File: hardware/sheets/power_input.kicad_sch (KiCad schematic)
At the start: 16 parts, among them J1 PWR (SS1.5 3-way), Q1 SQJ415EP

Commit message: hw(sch): Task 7 schematic review - three defects found and fixed
Every spec requirement traced to a sheet and refdes, read back from the
exported netlist rather than the drawing. 29 of 31 rows PASS; two carried
forward. Full write-up in hardware/docs/schematic-review.md.

F1 - Q1 carried the superseded SQJ415EP. That part was replaced by the
SQJ461EP on 2026-09-13 precisely because it is a 40 V device and the
SMBJ24A clamps at 38.9 V - 2.8% margin on the one part that sees every
vehicle transient. The replacement reached part-selection.md and the spec
but never the schematic, so a BOM built from it would have ordered the
wrong FET. Also closes the open gate-drive question: D1/R1 put Vgs at
-11 to -12.6 V, so the 16 mOhm column applies and the 0.78 W figure stands.

F2 - R2 and R3, the 0R links that short both windings of the common-mode
choke L2, were not marked DNP. A BOM would have stuffed the choke AND the
links; the links win and L2 becomes decorative. The board would work
perfectly and filter nothing, with no ERC or DRC check saying a word.
Both are now DNP, and gen_power_input.py learned to emit (dnp yes).

F3 - the 24 V feedback divider (115k/4.99k = 120k) conducts in deep sleep:
with the boost disabled, +24V still sits at ~12.35 V through L3 and D4, so
the divider drew 103 uA - larger than every other sleep contributor
combined, and absent from the spec 8.2 budget. Raised to 576k/24.9k, same
ratio, 20.5 uA. Revised budget ~94 uA typ / ~111 uA max against the 200 uA
target. C61 (10 pF, DNP) fitted as a Cff stuff option for the higher FB
impedance.

Carried forward: F4 (L1/L2 carry the full 7.0 A and have no thermal budget
- a 22 mOhm total DCR ceiling is now specified) and F5 (the spec's second
feed DNP footprints do not exist; needs a decision before Task 8 commits
to an outline).

Verification: ERC --severity-all --exit-code-violations exit=0, 0 errors,
0 warnings. 166 nets, unchanged by the fixes. DNP set read back from the
sheets: 31 parts. All six genera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
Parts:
- Q1: value SQJ415EP -> SQJ461EP
- R2, R3: now not fitted
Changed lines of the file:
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@@
 		(on_board yes)
 		(in_pos_files yes)
-		(dnp no)
+		(dnp yes)
 		(property "Reference" "R3"
 			(at 92.71 92.71 90)
@@
 			)
 		)
-		(property "Value" "SQJ415EP"
+		(property "Value" "SQJ461EP"
 			(at 44.45 88.9 90)
 			(show_name no)
@@
 		(on_board yes)
 		(in_pos_files yes)
-		(dnp no)
+		(dnp yes)
 		(property "Reference" "R2"
 			(at 74.93 65.41 90)

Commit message: hw(sch): L2 = Wurth WE-CMBNC 7448031002, L1 = 1.5 uH - decision applied to the schematic
Owner's call: the Wurth over the two ferrite candidates. It is the only
AEC-Q200 Grade 1 part of the three and the only one that leaves the thermal
budget real margin - 18.40 mOhm against F4's 22 mOhm ceiling (16.4%) versus
21.80 mOhm (0.9%) for either ferrite, 0.90 W instead of 1.07 W, night total
~2.70 W against the plate's ~2.9 W.

Applied to the DESIGN, not just the prose: layout_power_input.py now sets
L2 = 7448031002 and L1 = 1.5uH, replacing the "CM choke" and "10uH"
placeholders. This is exactly what finding F1 caught going wrong the other
way - the SQJ461EP was chosen on 2026-09-13, recorded in three documents, and
never reached the generator, so a BOM built from the schematic would have
ordered a 40 V part.

The coupling between L1 and L2 is now written into the generator as a comment,
because it is not visible from either value alone: F4 caps L1 plus BOTH L2
windings at 22 mOhm, and with either ferrite alternative a 2.2 uH L1 breaks
the ceiling. Nobody should change one without re-checking the other.

Verification: ERC --severity-all --exit-code-violations exit=0, 0 violations.
166 nets, unchanged - these are Value fields, not connectivity. L1 and L2 read
back from the netlist as 1.5uH and 7448031002.

Still carried, both flagged rather than assumed: whether the Wurth's 6.3 mOhm
is per winding (assumed - conservative) or total, and the derating curve at
the 65 C internal ambient since the 10 A is specified at 20 C.

Co-Authored-By: Claude Opus 5 <noreply@anthropic.com>
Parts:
- L1: value 10uH -> 1.5uH
- L2: value CM choke -> 7448031002
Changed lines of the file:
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@@
 			)
 		)
-		(property "Value" "10uH"
+		(property "Value" "1.5uH"
 			(at 107.95 82.55 90)
 			(show_name no)
@@
 			)
 		)
-		(property "Value" "CM choke"
+		(property "Value" "7448031002"
 			(at 88.9 69.85 0)
 			(show_name no)

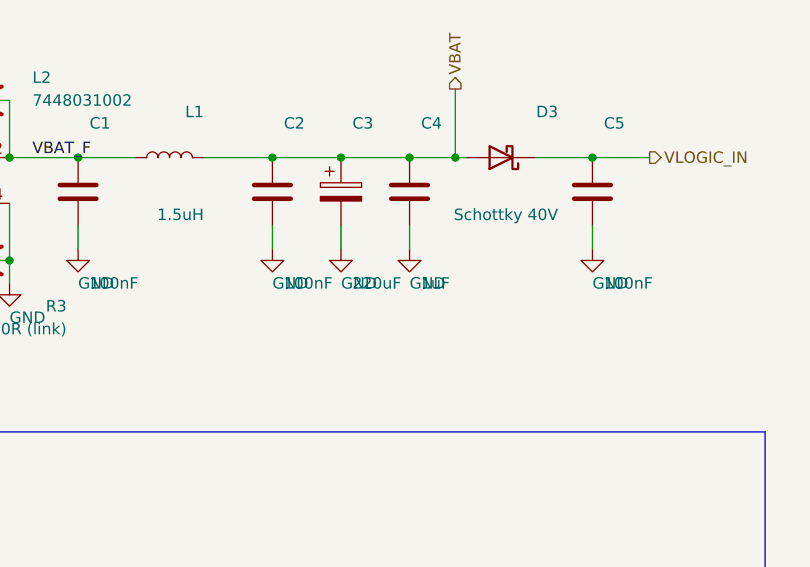
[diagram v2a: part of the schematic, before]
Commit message: hw(sch): sweep every selected part into the schematic; D6+D7 become one PESD2CANFD24U-T
Closes the gap the Task 7 review's finding F1 was about: parts chosen in
prose had not reached the generators, which is exactly how the superseded
SQJ415EP survived five days in the schematic.

STRUCTURAL - the CAN ESD pair is now one part. D6 and D7 were two placeholder
"24V bidir" discretes; the Nexperia PESD2CANFD24U-T is a single SOT23 holding
both bidirectional elements (K1/K2/CC). New verified symbol in symlib.py built
from Table 2 of the datasheet, added to gen_mcu_can's lib_symbols, and
Device:D_TVS dropped from that sheet since D6/D7 were its only users.

The two protected pins land exactly on the CANH and CANL runs, so each run is
drawn as TWO segments meeting AT the pin rather than one segment the pin
happens to touch. A pin sitting mid-wire does connect, but this project has
already produced one silent connectivity defect of that shape (labels
mid-wire, 14 instances), so the pin is made a wire endpoint and junctioned.
Verified from the netlist rather than from ERC: D6.1 -> /CANH, D6.2 -> /CANL,
D6.3 -> GND.

Consolidating freed D7, so the diode series was renumbered to stay gapless:
the ignition-divider BAT54 D8 -> D7, the twelve RGB sense clamps D9-D20 ->
D8-D19, and the PROFET sense clamp D21 -> D20. Every designator series is
gapless: C1-61, D1-20, F1-5, J1-8, L1-6, Q1-9, R1-99, SW1-2, U1-9.

VALUE SWEEP - L4/L5 "22uH" -> XAL7070-223ME, L6 "51uH CM choke" ->
ACT45B-510-2P-TL003, C3 "220uF" -> "220uF 63V" (the SMBJ24A's 8/20 us clamp is
50.6 V, so a 50 V part has no margin), U7 -> PCA9685PW/Q900, the only
AEC-Q100 variant in the ordering table. U7's lib_id stays Driver_LED:PCA9685PW
- that is the stock symbol's name, and the package is the same TSSOP28. D4 was
already SS5PH102.

FOOTPRINT - installed the vendor SamacSys footprint and STEP model for the
Wurth choke as footprints/mccan.pretty/Wurth_WE-CMBNC_7448031002.kicad_mod and
3dmodels/. Its pads verify against t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
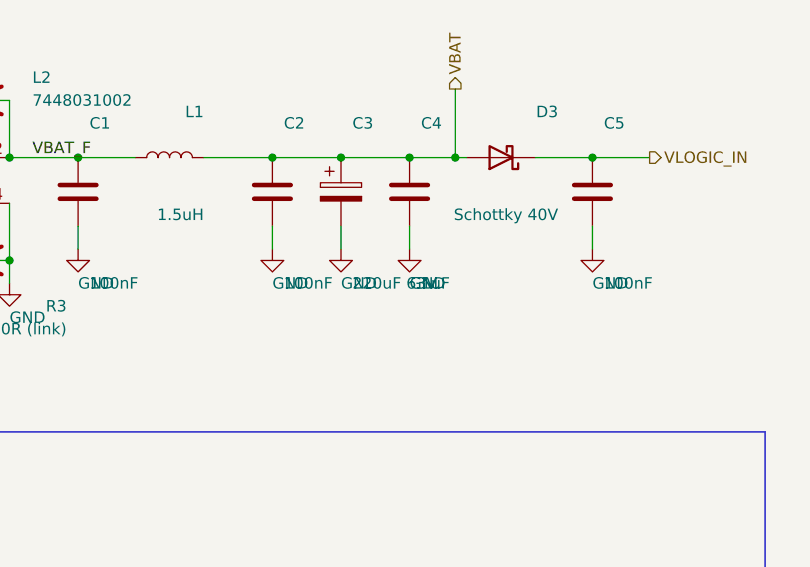
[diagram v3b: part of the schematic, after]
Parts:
- C3: value 220uF -> 220uF 63V
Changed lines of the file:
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@@
 			)
 		)
-		(property "Value" "220uF"
+		(property "Value" "220uF 63V"
 			(at 124.46 90.17 0)
 			(show_name no)

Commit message: hw(pcb): Task 8 step 0 - footprints assigned, 209 of 219 verified
Nothing in the project had a footprint except the PROFET's. Assignment now
lives in one auditable place, scripts/fpmap.py, which the four sheet
generators call when emitting each symbol's Footprint property. No generator
chooses a footprint of its own any more.

Three rules, and the reasoning is in the file rather than in a commit nobody
will read again: signal passives are 0603; a passive gets a bigger package
only for a stated reason; and nothing gets a footprint that has not been
checked to exist.

The reasons that drove a larger package:
- R2/R3, the 0R links bypassing the input choke windings, are 2512. They are
  DNP, but if anyone fits them for the tied-ground prototype they carry the
  entire 7.0 A night load, and a 0603 link is rated about 1 A.
- R52-R63, the RGB sense shunts, are 1206 for the FAULT case, not the normal
  7 mW. The package is sized on the understanding that firmware latches a
  shorted channel off; if that is ever dropped they must become 2512 1 W.
- The front-end ceramics are sized against the SMBJ24A's 8/20 us clamp of
  50.6 V, not the 38.9 V the distributor summaries quote. 100 nF fits 0805 at
  100 V; 1-2.2 uF at 63 V does not fit 0805; 10 uF at 63 V needs 1210.
- C20-C22 on +24 V are 1206 for DC-BIAS derating, a different reason - a 25 V
  X7R at 24 V keeps only 40-60% of nameplate.

Package identifications read from the datasheets rather than assumed:
NX5020UNBKS is SOT363/SC-88 (section 1), LM51571-Q1 RTE is WQFN-16 3x3 with a
1.66 mm exposed pad (so KiCad's EP1.675x1.675 is within tolerance), SS5PH102
is TO-277A, PESD2CANFD24U-T is SOT23.

FLAGGED, not silently accepted: the LM5164 DDA thermal pad is 3.4 x 2.8 mm on
the mechanical drawing and KiCad has no exact match. EP2.62x3.51 is the
closest by area (9.20 mm2 against 9.52) and is used for now, but that pad is
the part's heatsink on a thermally critical rail, so an exact DDA land pattern
should be drawn before fabr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
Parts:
- C1: footprint (none) -> Capacitor_SMD:C_0603_1608Metric
- C2, C5: footprint (none) -> Capacitor_SMD:C_0805_2012Metric
- C3: footprint (none) -> Capacitor_SMD:CP_Elec_10x10.5
- C4: footprint (none) -> Capacitor_SMD:C_1206_3216Metric
- D1: footprint (none) -> Diode_SMD:D_SOD-123
- D2: footprint (none) -> Diode_SMD:D_SMB
- D3: footprint (none) -> Diode_SMD:D_SMA
- L1: footprint (none) -> Inductor_SMD:L_Vishay_IHLP-4040
- L2: footprint (none) -> mccan:Wurth_WE-CMBNC_7448031002
- Q1: footprint (none) -> Package_SO:PowerPAK_SO-8L_Single
- R1: footprint (none) -> Resistor_SMD:R_0603_1608Metric
- R2, R3: footprint (none) -> Resistor_SMD:R_2512_6332Metric
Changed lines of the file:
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@@
 			)
 		)
-		(property "Footprint" ""
+		(property "Footprint" "Diode_SMD:D_SOD-123"
 			(at 62.23 85.09 0)
 			(hide yes)
@@
 			)
 		)
-		(property "Footprint" ""
+		(property "Footprint" "Capacitor_SMD:C_0603_1608Metric"
 			(at 93.98 80.01 0)
 			(hide yes)
@@
 			)
 		)
-		(property "Footprint" ""
+		(property "Footprint" "Diode_SMD:D_SMA"
 			(at 140.97 76.2 0)
 			(hide yes)
@@
 			)
 		)
-		(property "Footprint" ""
+		(property "Footprint" "Resistor_SMD:R_2512_6332Metric"
 			(at 81.28 87.63 0)
 			(hide yes)
@@
 			)
 		)
-		(property "Footprint" ""
+		(property "Footprint" "Capacitor_SMD:C_0805_2012Metric"
 			(at 151.13 80.01 0)
 			(hide yes)
@@
 			)
 		)
-		(property "Footprint" ""
+		(property "Footprint" "Resistor_SMD:R_0603_1608Metric"
 			(at 54.61 92.71 0)
 			(hide yes)
@@
 			)
 		)
-		(property "Footprint" ""
+		(property "Footprint" "Inductor_SMD:L_Vishay_IHLP-4040"
 			(at 104.14 76.2 0)
 			(hide yes)
@@
 			)
 		)
-		(property "Footprint" ""
+		(property "Footprint" "Capacitor_SMD:CP_Elec_10x10.5"
 			(at 123.19 80.01 0)
 			(hide yes)
@@
 			)
 		)
-		(property "Footprint" ""
+		(property "Footprint" "Capacitor_SMD:C_0805_2012Metric"
 			(at 115.57 80.01 0)
 			(hide yes)
@@
 			)
 		)
-		(property "Footprint" ""
+		(property "Footprint" "Package_SO:PowerPAK_SO-8L_Single"
 			(at 54.61 78.74 0)
 			(hide yes)
@@
 			)
 		)
-		(property "Footprint" ""
+		(property "Footprint" "Diode_SMD:D_SMB"
 			(at 66.04 80.01 0)
 			(hide yes)
@@
 			)
 		)
-		(property "Footprint" ""
+		(property "Footprint" "Resistor_SMD:R_2512_6332Metric"
 			(at 81.28 69.85 0)
 			(hide yes)
@@
 			)
 		)
-		(property "Footprint" ""
+		(property "Footprint" "Capacitor_SMD:C_1206_3216Metric"
 			(at 130.81 80.01 0)
 			(hide yes)
@@
 			)
 		)
-		(property "Footprint" ""
+		(property "Footprint" "mccan:Wurth_WE-CMBNC_7448031002"
 			(at 81.28 78.74 0)
 			(hide yes)

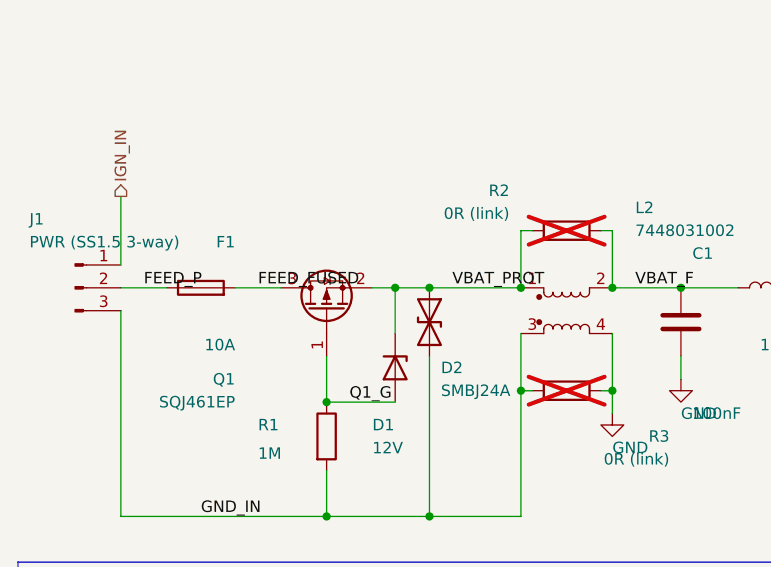
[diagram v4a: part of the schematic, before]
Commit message: hw(sch): CM chokes were wired to KiCad's pin numbering, not the parts'
Both common-mode chokes used Device:L_Coupled, which numbers its pins
winding A = 1-2, winding B = 3-4.  Every real four-terminal CM choke numbers
them winding A = 1-4, winding B = 2-3.  Both parts in this design are real
ones, so both were wired across the wrong pairs.

L2 was the serious one.  As drawn, winding 1-4 tied VBAT_PROT to board GND
and winding 2-3 tied VBAT_F to GND_IN -- two dead shorts across the supply
through 6.3 mOhm windings.  First power-up would have cleared the 10 A fuse
with the P-FET and the choke carrying the fault.

L6 transposed CANH and CANL between the transceiver and the connector, so the
board would never have received a frame.  Being listen-only by default, the
symptom is "no traffic" -- which spec 8.3 already names as the top risk and
the thing most likely to be misdiagnosed as a firmware fault.

ERC passes either way.  DRC passes either way.  The footprint pad count
matches either way.  Nothing automated catches this.

Verified from the VECTOR GEOMETRY of both datasheets, not a text dump -- a
flat extraction gives four bare numerals with no axis:
  Wurth WE-CMBNC 7448031002 "Schematic": upper coil's leads sit under labels
    1 (x=347.0) and 4 (x=488.6); lower coil's under 2 and 3 at the same x.
  TDK ACT45B "CIRCUIT DIAGRAM": identical, 1/4 upper, 2/3 lower.

Fix is a mccan_parts:CM_CHOKE_4T symbol drawn with L_Coupled's own graphics
but numbered to match the parts.  Not one wire moves -- which is also why the
drawing never looked wrong.  Netlist now reads:
  L2.1->4  VBAT_PROT -> VBAT_F      L2.2->3  GND_IN -> GND
  L6.1->4  U6 CANH   -> CANH        L6.2->3  U6 CANL -> CANL

Also in this commit, from the two datasheets supplied today:

- Superseal is a WIRE-TO-WIRE series with no panel-mount board-side housing,
  so the seven "panel connectors" could never have been built, and that is
  why all seven sat in fpmap.BLOCKED through Task 8 step 0.  J1 and J3-J8
  b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
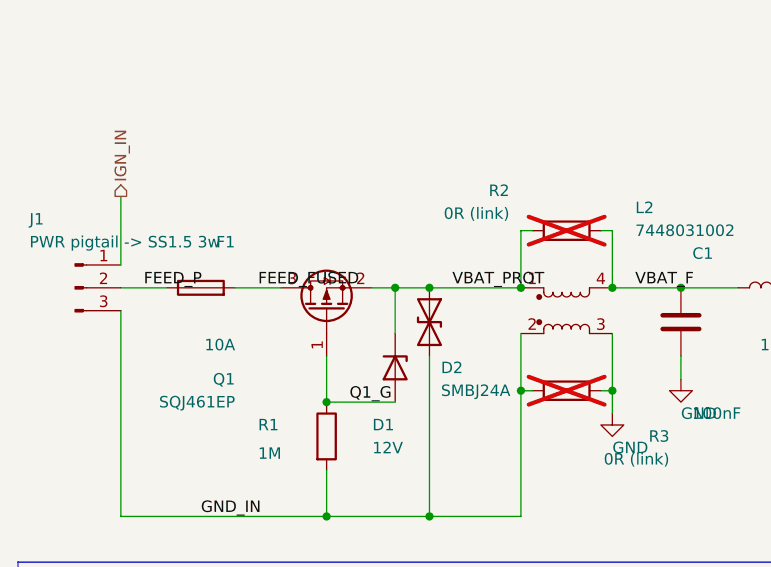
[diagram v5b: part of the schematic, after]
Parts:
- J1: value PWR (SS1.5 3-way) -> PWR pigtail -> SS1.5 3w; footprint (none) -> Connector_Wire:SolderWire-1.5sqmm_1x03_P6mm_D1.7mm_OD3mm_Relief
- L2: symbol Device:L_Coupled -> mccan_parts:CM_CHOKE_4T
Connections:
- net GND: now also L2.3; no longer L2.4
- net GND_IN: now also L2.2; no longer L2.3
- net VBAT_F: now also L2.4; no longer L2.2
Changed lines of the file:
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@@
 			)
 		)
-		(property "Value" "PWR (SS1.5 3-way)"
+		(property "Value" "PWR pigtail -> SS1.5 3w"
 			(at 21.59 71.12 0)
 			(show_name no)
@@
 			)
 		)
-		(property "Footprint" ""
+		(property "Footprint" "Connector_Wire:SolderWire-1.5sqmm_1x03_P6mm_D1.7mm_OD3mm_Relief"
 			(at 26.67 76.2 0)
 			(hide yes)
@@
 	)
 	(symbol
-		(lib_id "Device:L_Coupled")
+		(lib_id "mccan_parts:CM_CHOKE_4T")
 		(at 81.28 78.74 0)
 		(unit 1)

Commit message: hw(sch): spec 4.2 built - LTC4380 eFuse replaces F1/Q1/D1/R1
The input stage's fuse, P-FET, gate Zener and gate pull-down are gone. In
their place: U10 (LTC4380-2) driving a back-to-back pass pair Q10/Q11 across
R100, doing reverse polarity, current limit and overvoltage clamp in one
conduction path. Night falls 2.70 W -> 2.31 W.

Built from the datasheet's Figure 7, not Figure 5 - only R_SNS, R_DRN and
C_TMR are rescaled. Two deliberate departures, both noted on the sheet:
R103/C64 are the PIN FUNCTIONS minimum (33R/47nF) rather than Figure 7's
drawn 150R/0.1uF, because a larger C64 pushes the fault timeout past the SOA
curve that was checked; and ON/FLT are left open under no-connect flags.

THE PASS PAIR IS COMMON DRAIN. Verified by hand against the generated
netlist, which is what spec 4.2 makes the acceptance criterion:

  FEED_P     J1.2 Q10.2 Q12.2 R104.1 R105.1
  MID        Q10.3 Q11.3 R101.1
  SNS        Q11.2 R100.1 U10.4

Drains (pin 3) meet at MID, sources (pin 2) face outward. Wired common
source the board passes ERC, DRC and the pad count with no reverse-polarity
protection at all.

RENUMBERED. Spec 4.2 named its parts R88-R95, C49-C52 and D22-D24; every one
was taken - R88-R99 and C49-C61 are the RGB output snubbers. Built as
R100-R107, C62-C65 and D21-D23, and the spec now carries the mapping table.

C65 (22 uF at OUT) is new: PIN FUNCTIONS requires it and nothing else on the
sheet satisfied it. No orderable yet - flagged, along with Q12, D21-D23 and
the HSOF-8 variant for Q10/Q11.

Sheet moved to A3 and the input filter shifted 73.66 mm right to make room.
Note boxes now stack automatically in two columns rather than by hand.

ERC: 0 violations. Footprints: 233 verified, 0 failures, U4 still blocked.

Co-Authored-By: Claude Opus 5 <noreply@anthropic.com>
Claude-Session: https://claude.ai/code/session_01Bkq7QP4he4cdfxkUNzx7DL
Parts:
- removed D1: 12V, Diode_SMD:D_SOD-123, symbol Device:D_Zener
- removed F1: 10A, symbol Device:Fuse
- removed Q1: SQJ461EP, Package_SO:PowerPAK_SO-8L_Single, symbol Transistor_FET:Q_PMOS_GSD
- removed R1: 1M, Resistor_SMD:R_0603_1608Metric, symbol Device:R
- added C62: 680nF, Capacitor_SMD:C_0603_1608Metric, symbol Device:C
- added C63: 220nF, Capacitor_SMD:C_0603_1608Metric, symbol Device:C
- added C64: 47nF, Capacitor_SMD:C_0805_2012Metric, symbol Device:C
- added C65: 22uF 63V, Capacitor_SMD:CP_Elec_6.3x7.7, symbol Device:C_Polarized
- added D21: 22V, Diode_SMD:D_SOD-123, symbol Device:D_Zener
- added D22, D23: 1N4148, Diode_SMD:D_SOD-323, symbol Device:D
- added Q10, Q11: IPT008N06NM5LF, Package_TO_SOT_SMD:Infineon_PG-HSOF-8-1, symbol Transistor_FET:Q_NMOS_GSD
- added Q12: MMBT3904, Package_TO_SOT_SMD:SOT-23, symbol Transistor_BJT:Q_NPN_BEC
- added R100: 5m6 1% 1W, Resistor_SMD:R_2512_6332Metric, symbol Device:R
- added R101: 30k, Resistor_SMD:R_1206_3216Metric, symbol Device:R
- added R102: 10R, Resistor_SMD:R_0603_1608Metric, symbol Device:R
- added R103: 33R, Resistor_SMD:R_0603_1608Metric, symbol Device:R
- added R104, R106: 10k, Resistor_SMD:R_0603_1608Metric, symbol Device:R
- added R105, R107: 240k, Resistor_SMD:R_1206_3216Metric, symbol Device:R
- added U10: LTC4380HMS-2, Package_SO:MSOP-10_3x3mm_P0.5mm, symbol mccan_parts:LTC4380
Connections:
- net FEED_P: now also Q10.2 (S), Q12.2 (E), R104.1, R105.1
- net GND_IN: now also C62.2, C63.2, C64.2, C65.2, D21.2 (A), D23.2 (A), U10.6 (SEL), U10.8 (GND)
- net VBAT_PROT: now also C65.1, R100.2, U10.5 (OUT)
- new net: D23.1 (K), R106.2
- new net: D22.2 (A), R107.1
- new net: C62.1, U10.10 (TMR)
- new net: Q11.1 (G), R102.1
- new net: Q12.1 (B), R105.2, R106.1
- new net: C64.1, R103.2
- new net MID: Q10.3 (D), Q11.3 (D), R101.1
- new net Q10_G: D22.1 (K), Q10.1 (G), Q12.3 (C)
- new net SNS: Q11.2 (S), R100.1, U10.4 (SNS)
- new net U10_DRN: R101.2, U10.1 (DRN)
- new net U10_GATE: R102.2, R103.1, R107.2, U10.3 (GATE)
- new net VCC10: C63.1, D21.1 (K), R104.2, U10.2 (VCC)
- no-connect marks 0 -> 2
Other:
- moved on the sheet: C1, C2, C3, C4, C5, D2, D3, L1, L2, R2, R3
